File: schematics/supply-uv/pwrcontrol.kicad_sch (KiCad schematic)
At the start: 33 parts, among them J6 USBASP, J7 JST XH B3B, J8 Conn_01x03_Pin, Q13 IRLML0030, Q14 IRLML0030, SW1 SW_Push, U21 TL431DBZ, U22 ATtiny1616-M

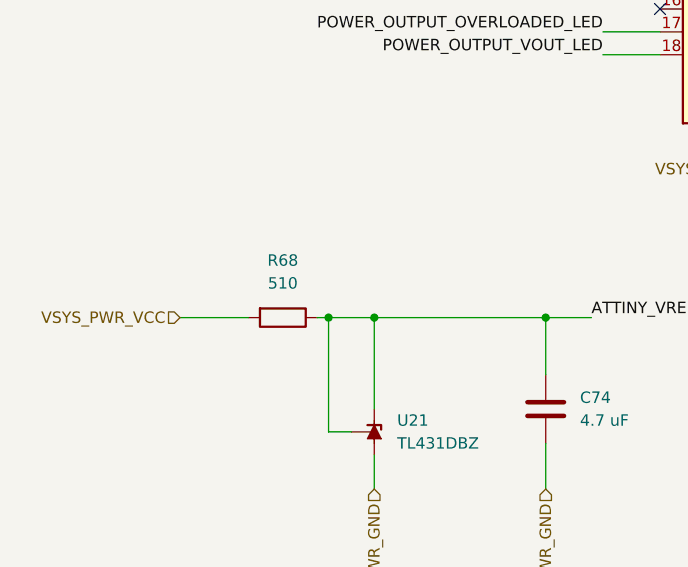
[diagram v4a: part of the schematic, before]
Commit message: power board works (except power output driver, not tested yet), I ready to solder control board
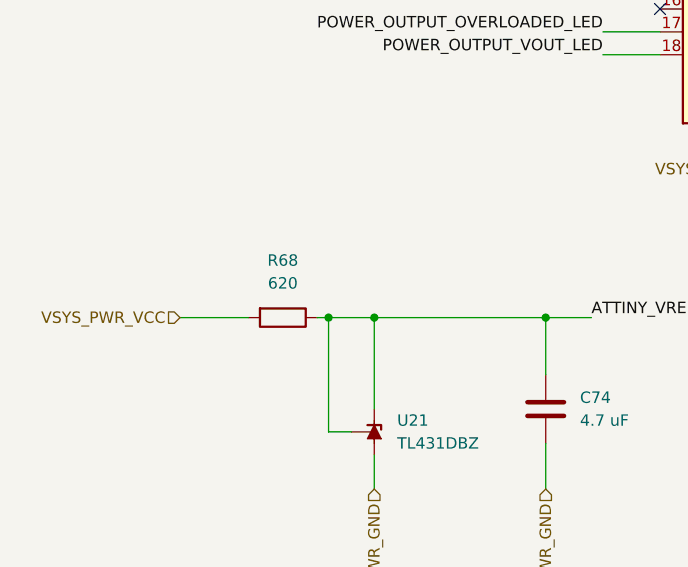
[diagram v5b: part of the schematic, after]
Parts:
- R68: value 510 -> 620
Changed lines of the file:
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@@
 	(label "POWER_OUTPUT_VOUT_LED"
 		(at 270.51 162.56 180)
-		(fields_autoplaced yes)
 		(effects
 			(font
@@
 	(label "ATTINY_TXD"
 		(at 156.21 124.46 0)
-		(fields_autoplaced yes)
 		(effects
 			(font
@@
 	(label "ATTINY_VREF_2V5"
 		(at 219.71 85.09 180)
-		(fields_autoplaced yes)
 		(effects
 			(font
@@
 	(label "ATTINY_TXD"
 		(at 233.68 40.64 0)
-		(fields_autoplaced yes)
 		(effects
 			(font
@@
 	(label "POWER_OUTPUT_IC_FB"
 		(at 477.52 121.92 180)
-		(fields_autoplaced yes)
 		(effects
 			(font
@@
 	(label "POWER_OUTPUT_IC_FB"
 		(at 149.86 109.22 0)
-		(fields_autoplaced yes)
 		(effects
 			(font
@@
 	(label "IS_ONOFF_BUTTON_PRESSED"
 		(at 149.86 106.68 0)
-		(fields_autoplaced yes)
 		(effects
 			(font
@@
 	(label "POWER_OUTPUT_OVERLOADED_LED"
 		(at 107.95 124.46 180)
-		(fields_autoplaced yes)
 		(effects
 			(font
@@
 	(label "ATTINY_VREF_2V5"
 		(at 106.68 156.21 0)
-		(fields_autoplaced yes)
 		(effects
 			(font
@@
 	(label "ATTINY_RXD"
 		(at 233.68 38.1 0)
-		(fields_autoplaced yes)
 		(effects
 			(font
@@
 	(label "POWER_OUTPUT_VOUT_LED"
 		(at 107.95 127 180)
-		(fields_autoplaced yes)
 		(effects
 			(font
@@
 	(label "ATTINY_RESET#"
 		(at 213.36 40.64 180)
-		(fields_autoplaced yes)
 		(effects
 			(font
@@
 	(label "POWER_OUTPUT_OVERLOADED_LED"
 		(at 207.01 160.02 180)
-		(fields_autoplaced yes)
 		(effects
 			(font
@@
 	(label "IS_ONOFF_BUTTON_PRESSED"
 		(at 486.41 78.74 180)
-		(fields_autoplaced yes)
 		(effects
 			(font
@@
 	(label "ATTINY_RXD"
 		(at 156.21 127 0)
-		(fields_autoplaced yes)
 		(effects
 			(font
@@
 	(label "ATTINY_RESET#"
 		(at 149.86 69.85 180)
-		(fields_autoplaced yes)
 		(effects
 			(font
@@
 	(label "ATTINY_VREF_2V5"
 		(at 149.86 111.76 0)
-		(fields_autoplaced yes)
 		(effects
 			(font
@@
 		(shape input)
 		(at 129.54 85.09 90)
-		(fields_autoplaced yes)
 		(effects
 			(font
@@
 		(shape input)
 		(at 234.95 45.72 0)
-		(fields_autoplaced yes)
 		(effects
 			(font
@@
 		(shape input)
 		(at 129.54 139.7 180)
-		(fields_autoplaced yes)
 		(effects
 			(font
@@
 		(shape input)
 		(at 234.95 33.02 0)
-		(fields_autoplaced yes)
 		(effects
 			(font
@@
 		(shape input)
 		(at 149.86 132.08 0)
-		(fields_autoplaced yes)
 		(effects
 			(font
@@
 		(shape input)
 		(at 151.13 82.55 0)
-		(fields_autoplaced yes)
 		(effects
 			(font
@@
 		(shape input)
 		(at 447.04 93.98 180)
-		(fields_autoplaced yes)
 		(effects
 			(font
@@
 		(shape input)
 		(at 463.55 105.41 180)
-		(fields_autoplaced yes)
 		(effects
 			(font
@@
 		(shape input)
 		(at 83.82 223.52 180)
-		(fields_autoplaced yes)
 		(effects
 			(font
@@
 		(shape input)
 		(at 149.86 114.3 0)
-		(fields_autoplaced yes)
 		(effects
 			(font
@@
 		(shape input)
 		(at 95.25 99.06 180)
-		(fields_autoplaced yes)
 		(effects
 			(font
@@
 		(shape input)
 		(at 290.83 128.27 180)
-		(fields_autoplaced yes)
 		(effects
 			(font
@@
 		(shape input)
 		(at 527.05 111.76 0)
-		(fields_autoplaced yes)
 		(effects
 			(font
@@
 		(shape input)
 		(at 82.55 175.26 270)
-		(fields_autoplaced yes)
 		(effects
 			(font
@@
 		(shape input)
 		(at 95.25 86.36 90)
-		(fields_autoplaced yes)
 		(effects
 			(font
@@
 		(shape input)
 		(at 288.29 172.72 270)
-		(fields_autoplaced yes)
 		(effects
 			(font
@@
 		(shape input)
 		(at 219.71 116.84 180)
-		(fields_autoplaced yes)
 		(effects
 			(font
@@
 		(shape input)
 		(at 101.6 175.26 270)
-		(fields_autoplaced yes)
 		(effects
 			(font
@@
 		(shape input)
 		(at 60.96 156.21 180)
-		(fields_autoplaced yes)
 		(effects
 			(font
@@
 		(shape input)
 		(at 149.86 129.54 0)
-		(fields_autoplaced yes)
 		(effects
 			(font
@@
 		(shape input)
 		(at 224.79 168.91 270)
-		(fields_autoplaced yes)
 		(effects
 			(font
@@
 		(shape input)
 		(at 149.86 121.92 0)
-		(fields_autoplaced yes)
 		(effects
 			(font
@@
 		(shape input)
 		(at 149.86 119.38 0)
-		(fields_autoplaced yes)
 		(effects
 			(font
@@
 		(shape input)
 		(at 519.43 123.19 270)
-		(fields_autoplaced yes)
 		(effects
 			(font
@@
 		(shape input)
 		(at 219.71 106.68 180)
-		(fields_autoplaced yes)
 		(effects
 			(font
@@
 		(shape input)
 		(at 486.41 133.35 270)
-		(fields_autoplaced yes)
 		(effects
 			(font
@@
 		(shape input)
 		(at 219.71 96.52 180)
-		(fields_autoplaced yes)
 		(effects
 			(font
@@
 		(shape input)
 		(at 171.45 73.66 90)
-		(fields_autoplaced yes)
 		(effects
 			(font
@@
 			)
 		)
-		(property "Value" "510"
+		(property "Value" "620"
 			(at 72.39 152.4 90)
 			(effects
@@
 		(on_board yes)
 		(dnp no)
-		(fields_autoplaced yes)
 		(property "Reference" "J7"
 			(at 300.99 129.54 0)
